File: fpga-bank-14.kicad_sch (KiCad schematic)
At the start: 2 parts, among them U1 XC7K410T-2FFG900I

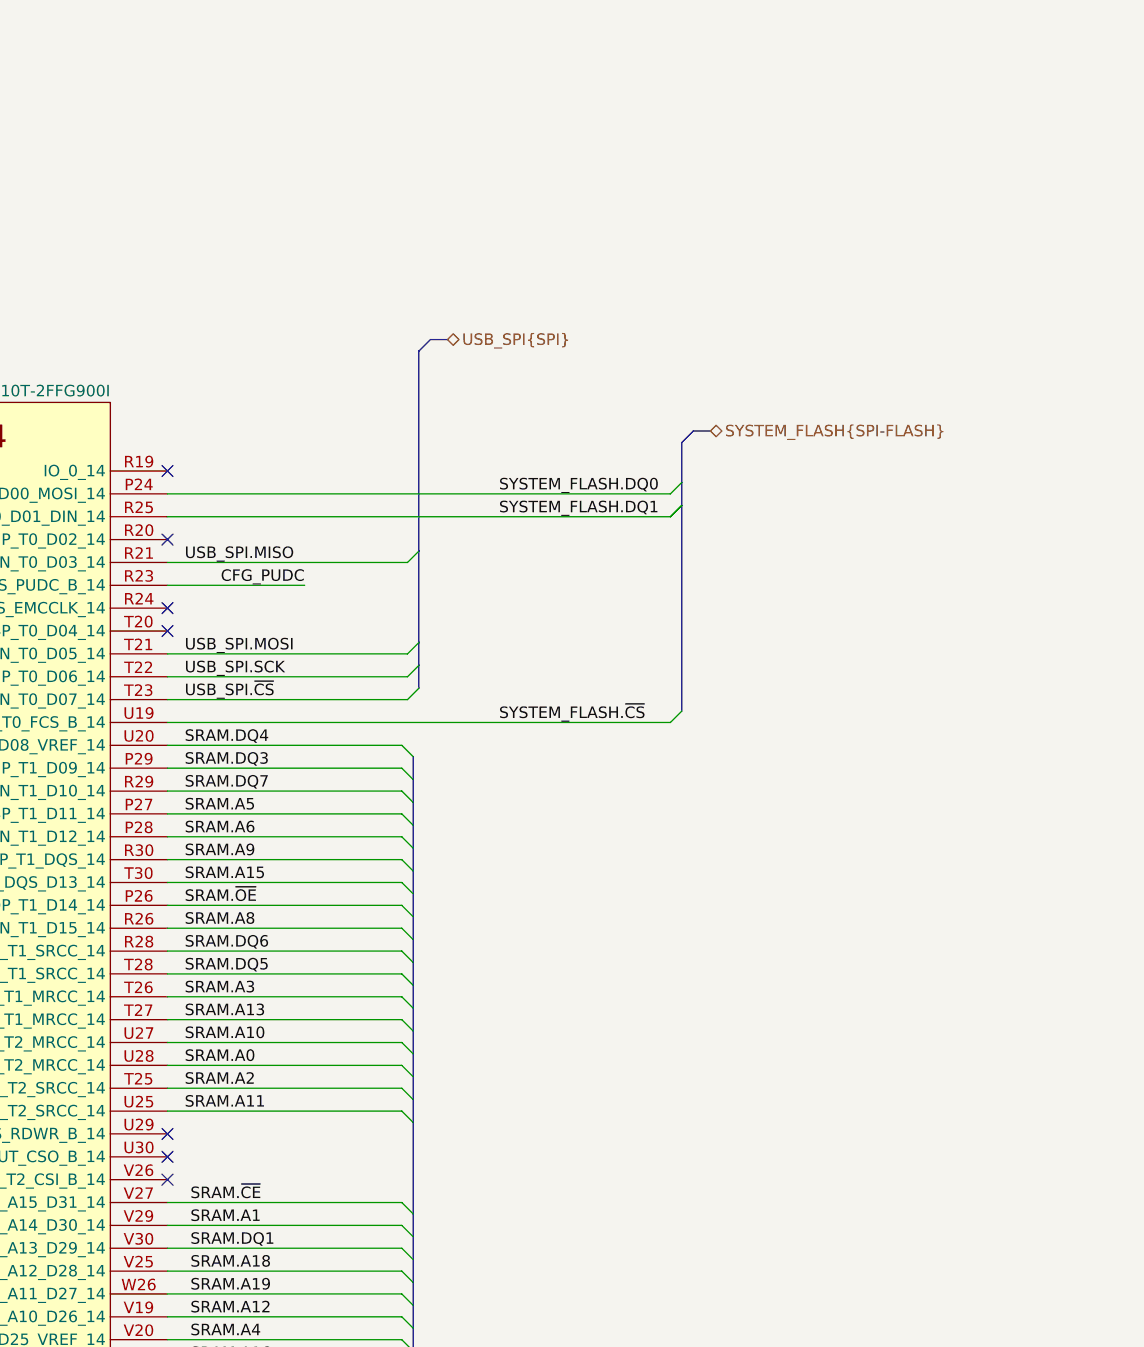
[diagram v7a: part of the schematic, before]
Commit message: Add new pinout to sup MCU. Start connecting it to FPGA
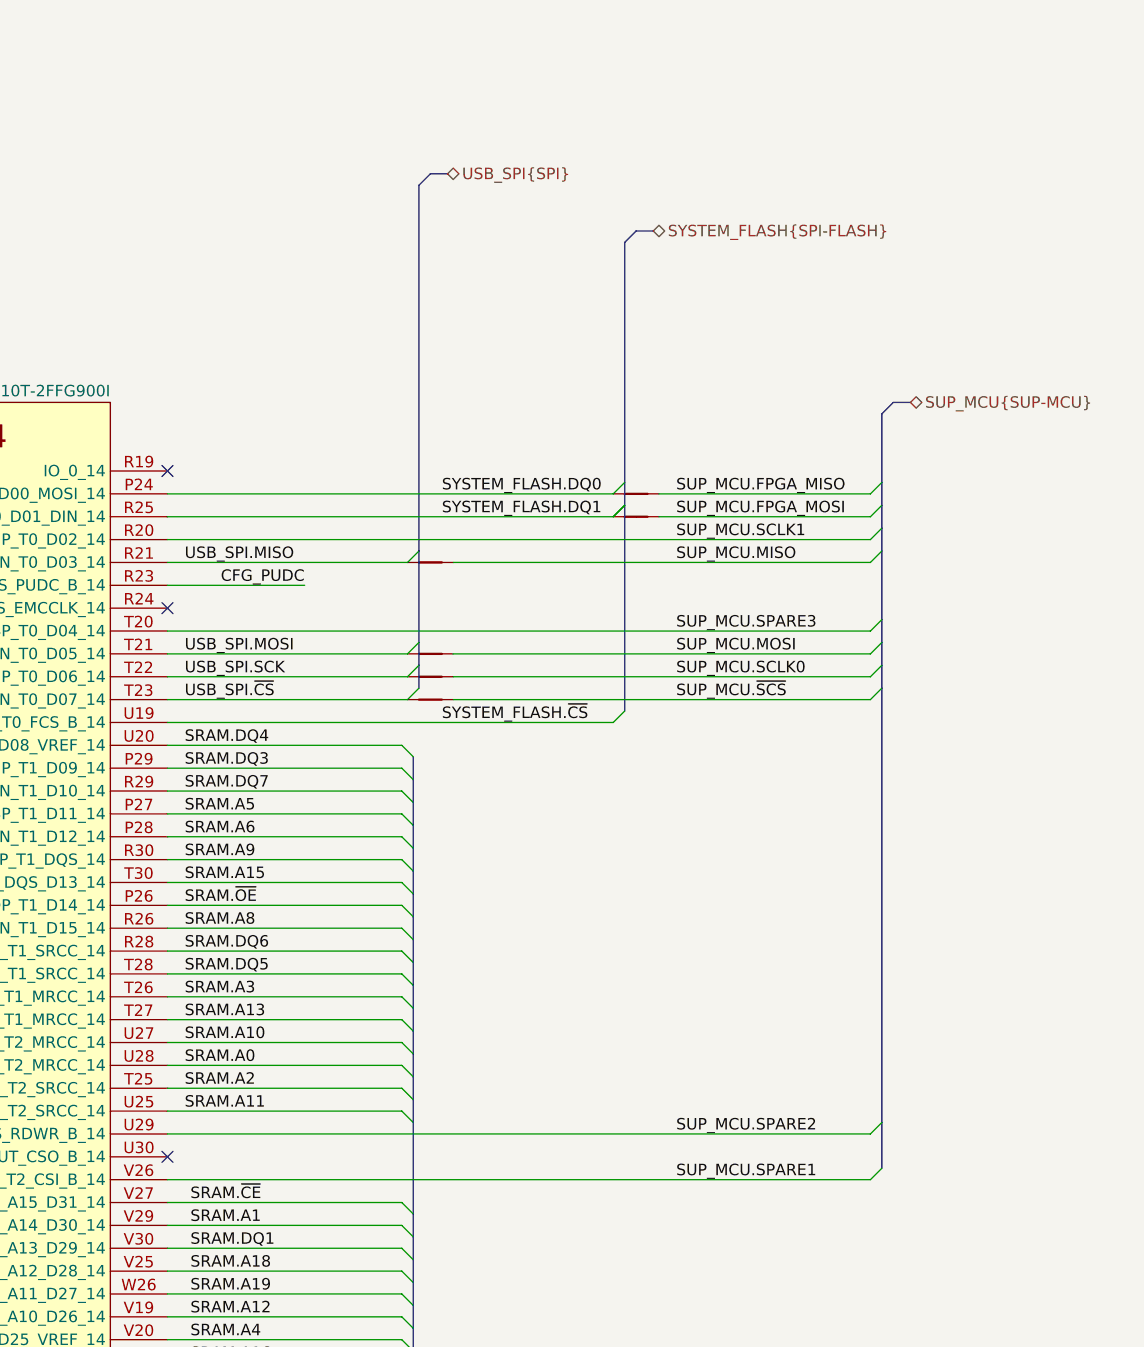
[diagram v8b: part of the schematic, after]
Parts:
- added NT? (x6): NetTie_2, antmicro-footprints:NetTie-2_SMD_Pad0.127mm, symbol antmicroShuntsJumpers:NetTie_2
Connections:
- net SYSTEM_FLASH.DQ0: now also NT?.1
- net SYSTEM_FLASH.DQ1: now also NT?.1
- net USB_SPI.MISO: now also NT?.1
- net USB_SPI.MOSI: now also NT?.1
- net USB_SPI.SCK: now also NT?.1
- net USB_SPI.~{CS}: now also NT?.1
- net SUP_MCU.SCLK1: now reaches U1.R20 (IO_L2P_T0_D02_14)
- net SUP_MCU.SPARE3: now reaches U1.T20 (IO_L4P_T0_D04_14)
- net SUP_MCU.SPARE2: now reaches U1.U29 (IO_L15P_T2_DQS_RDWR_B_14)
- net SUP_MCU.SPARE1: now reaches U1.V26 (IO_L16P_T2_CSI_B_14)
- new net SUP_MCU.FPGA_MISO: NT?.2
- new net SUP_MCU.FPGA_MOSI: NT?.2
- new net SUP_MCU.MISO: NT?.2
- new net SUP_MCU.MOSI: NT?.2
- new net SUP_MCU.SCLK0: NT?.2
- new net SUP_MCU.~{SCS}: NT?.2
- no-connect marks 10 -> 6
